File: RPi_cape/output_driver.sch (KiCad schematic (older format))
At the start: 18 parts, among them U8 74LVC1G08, U9 TPS1H100B

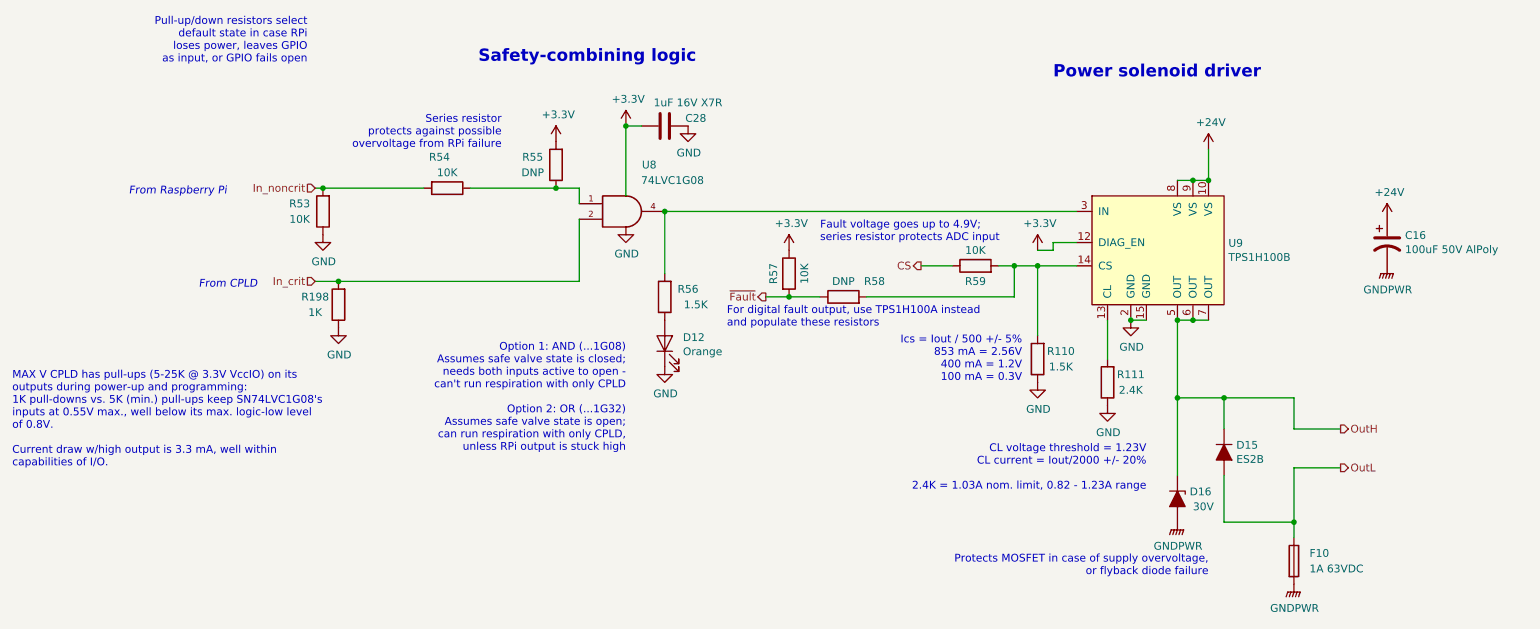
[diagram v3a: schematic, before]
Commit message: Design update based on changed software/firmware/pneumatics reqs
Swapped Max V CPLD for Max 10 FPGA
Removed +1.8V regulator and monitoring (in power-down alarm) because Max 10 FPGA has internal regulator
Changed FPGA's valve-enable pull-downs from 1K to 10K because Max 10 floats the outputs during power-up/programming (instead of Max V's internal pull-ups)
Changed low-pressure sensor from BMP388 to MS5607 for more manufacturable footprint / high availability, and moved all digital pressure sensors to daughterboard for repairability
Changed single op-amps in analog pressure sensor inputs / valve motion detect circuits to TLV6001 for better bias current, correct footprint
Removed excessive DNP components in analog pressure sensor inputs to ease routing with new op-amps
Added double-inverted hysteresis circuit to valve motion detect that won't drive U38's '+' input above the rail and cause latchup
Added optional pull-down resistors to valve-motiion-detect op-amps to allow output voltages to swing to zero
Added optional filter caps to ADC sensor inputs
Added pull-down to O2 sensor input for testing with sensor unplugged
Increased ADC input resistors (in analog sensor inputs) from 1K to 3.3K to avoid "lifting" +3.3V rail voltage in case of fault
Increased hole sizes to 3.7 mm for fitting #6 screws, to match some threaded vibration-damping bumpers from Joost
Fixed F.Fab-layer component reference text in custom footprints
Updated manufacturing files
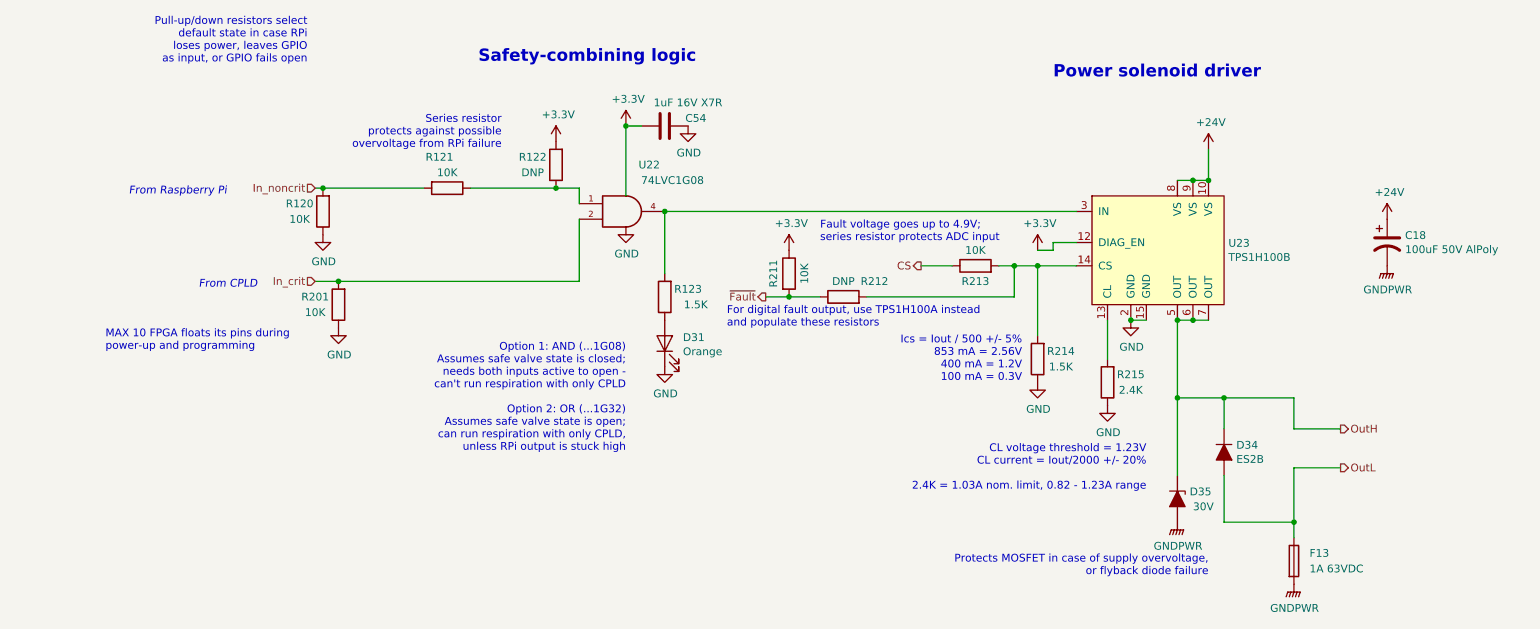
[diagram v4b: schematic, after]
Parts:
- R198: value 1K -> 10K; Part Number RK73H2BTTD1001F -> RK73H2BTTD1002F
- R55, R58: DNI (none) -> DNI
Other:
- note added: "MAX 10 FPGA floats its pins during\npower-up and programming"
- note removed: "MAX V CPLD has pull-ups (5-25K @ 3.3V VccIO) on its\noutputs during power-up and programming:\n1K pull-downs vs. 5K (min.) pull-ups keep SN74LVC1G08's\ninputs at 0.55V max., well below its max. logic-low level\nof 0.8V.\n\nCurrent draw w/high output is 3.3 mA, well within\ncapabilities of I/O."
